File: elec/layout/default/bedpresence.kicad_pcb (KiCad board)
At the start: 2 copper layers, 21 parts, among them U1 ?, U10 ?, U11 ?, U12 ?, U13 ?, U2 ?, U3 ?, U4 ?, U5 ?, U6 ?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

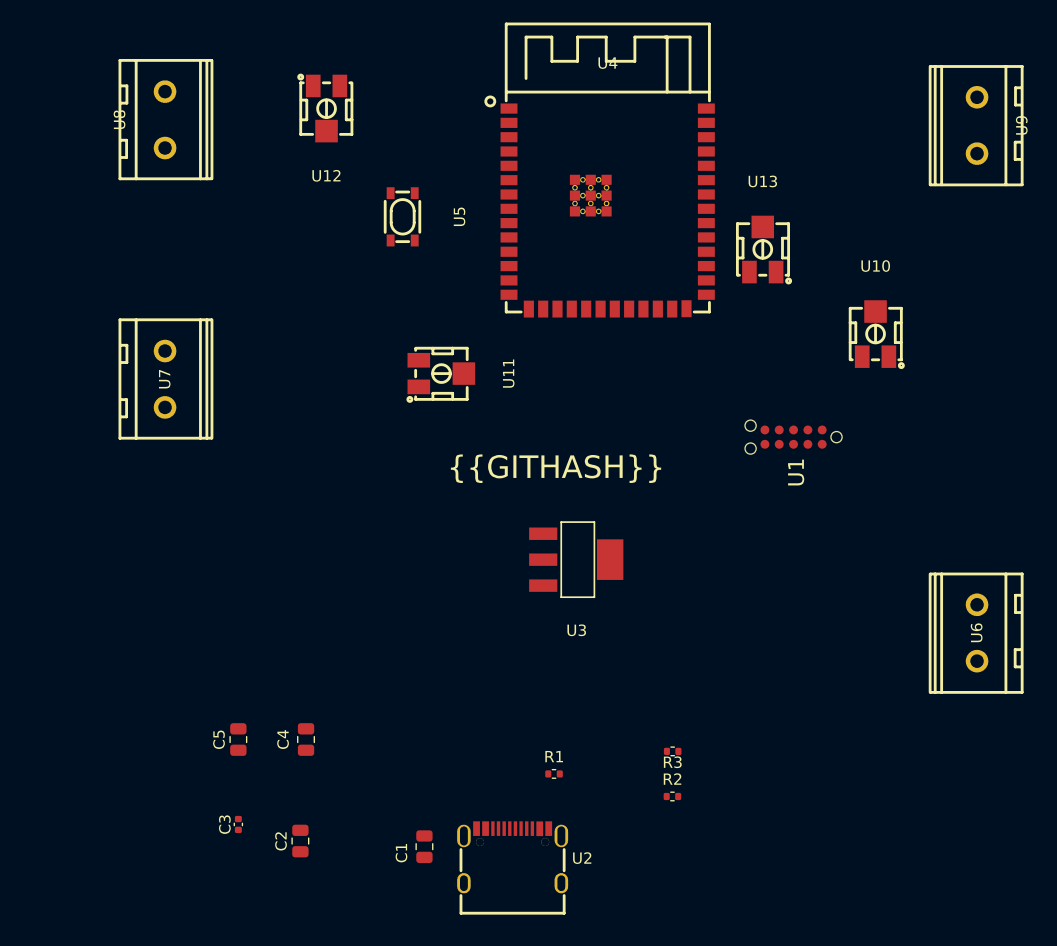
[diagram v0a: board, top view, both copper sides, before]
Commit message: Switch to digital potentiometers.
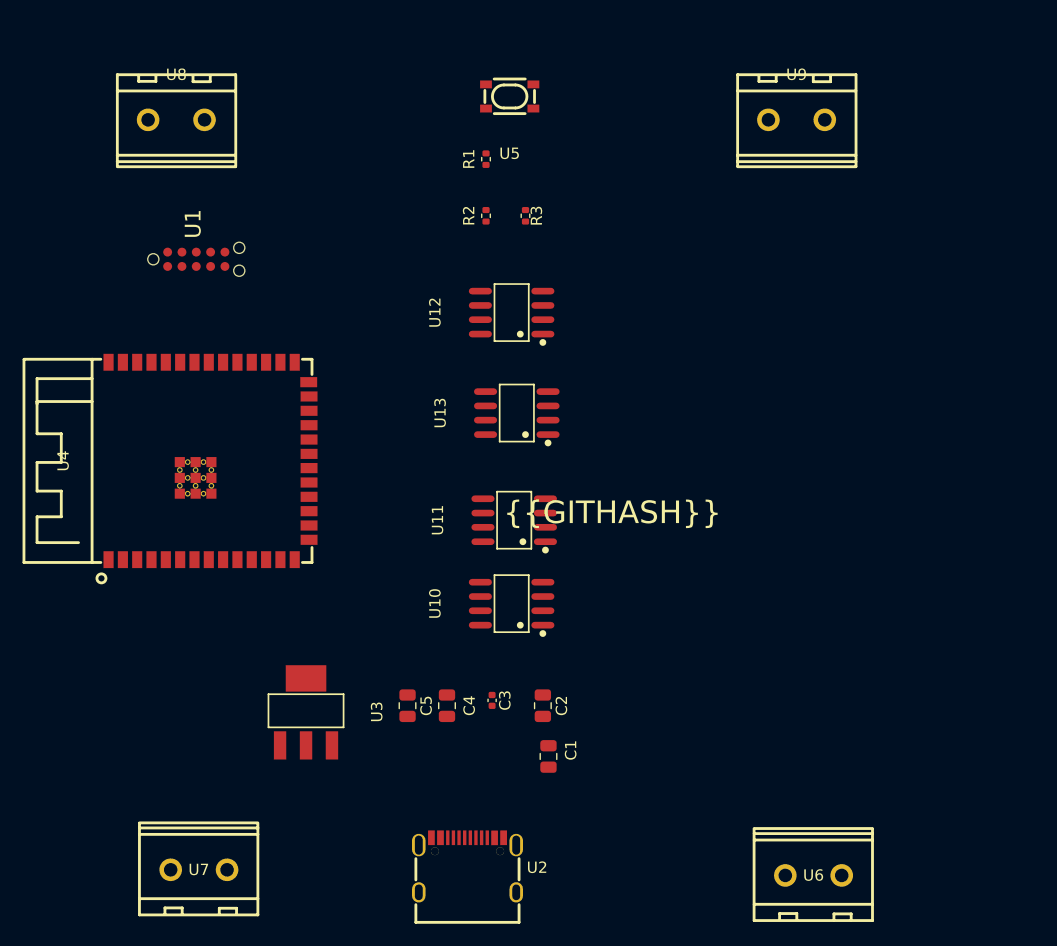
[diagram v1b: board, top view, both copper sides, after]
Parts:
- U10, U11, U12, U13: footprint lib:RES-ADJ-SMD_3314J -> lib:SOIC-8_L4.9-W3.9-P1.27-LS6.0-BL
- moved U1 55.3 mm to (125.8, 29.4), turned to 0 degrees
- moved R1 54.8 mm to (151.5, 20.5), turned to 90 degrees
- moved R2 54.1 mm to (151.5, 25.5), turned to 90 degrees
- moved R3 49.3 mm to (155.0, 25.5), turned to 90 degrees
- moved U7 43.6 mm to (126.0, 83.5), turned to 180 degrees
- moved U4 41.8 mm to (126.9, 47.2), turned to 90 degrees
- moved U10 40.2 mm to (153.7, 59.9), turned to 90 degrees
- moved U3 27.5 mm to (135.5, 69.5), turned to -90 degrees
- moved U13 26.2 mm to (154.2, 43.0), turned to 90 degrees
- moved U6 25.9 mm to (180.5, 84.0), turned to 180 degrees
- moved C3 25.0 mm to (152.0, 68.5), turned to -90 degrees
- moved C2 24.6 mm to (156.5, 69.0), turned to -90 degrees
- moved U12 24.4 mm to (153.7, 34.1), turned to 90 degrees
- moved U9 16.0 mm to (179.0, 17.0), turned to 0 degrees
- moved C5 15.3 mm to (144.5, 69.0), turned to -90 degrees
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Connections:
- U10 pad 1: vcc-1 -> micro.ic-cs
- U10 pad 2: micro.ic-_1 -> sck
- U10 pad 3: gnd-1 -> mosi
- U11 pad 1: vcc-1 -> micro.ic-cs-3
- U11 pad 2: io6 -> sck
- U11 pad 3: gnd-1 -> mosi
- U12 pad 1: vcc-1 -> micro.ic-cs-2
- U12 pad 2: connector3-_1 -> sck
- U12 pad 3: gnd-1 -> mosi
- U13 pad 1: vcc-1 -> micro.ic-cs-1
- U13 pad 2: connector4-_1 -> sck
- U13 pad 3: gnd-1 -> mosi
- U4 pad 10: io17 -> micro.ic-cs-1
- U4 pad 19: io11 -> micro.ic-cs
- U4 pad 20: io12 -> sck
- U4 pad 21: io13 -> mosi
- U4 pad 4: micro.ic-_1 -> io4
- U4 pad 5: io6 -> io5
- U4 pad 7: io6 -> io7
- U4 pad 8: io15 -> micro.ic-cs-3
- U4 pad 9: io16 -> micro.ic-cs-2
- U6 pad 1: micro.ic-_1 -> connector1-_1
- U7 pad 1: io6 -> connector2-_1
